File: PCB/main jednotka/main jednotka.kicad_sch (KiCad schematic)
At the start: 3 parts

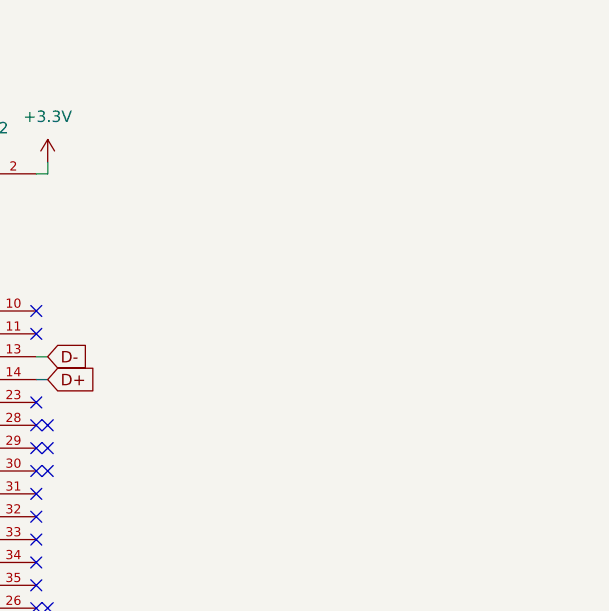
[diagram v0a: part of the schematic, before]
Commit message: USB-C + ESP32 modely added
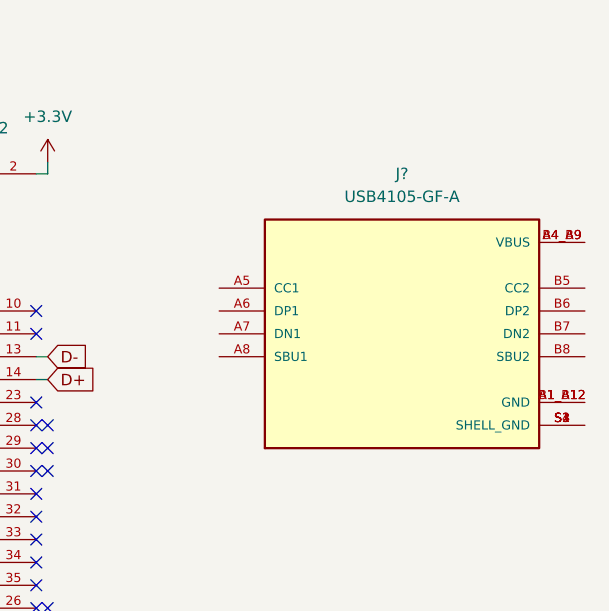
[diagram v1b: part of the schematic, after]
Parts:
- added J?: USB4105-GF-A, USB-C better:GCT_USB4105-GF-A, symbol USB4105-GF-A:USB4105-GF-A
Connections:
- new net: J?.A1_B12 (GND), J?.B1_A12 (GND)
- new net: J?.A4_B9 (VBUS), J?.B4_A9 (VBUS)
- new net: J?.S1 (SHELL_GND), J?.S2 (SHELL_GND), J?.S3 (SHELL_GND), J?.S4 (SHELL_GND)
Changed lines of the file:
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@@
     (pin "2")
+  )
+  (symbol (lib_id "USB4105-GF-A:USB4105-GF-A") (at 247.65 83.82 0) (unit 1)
+    (in_bom yes) (on_board yes) (fields_autoplaced)
+    (property "Reference" "J?" (id 0) (at 247.65 66.04 0))
+    (property "Value" "USB4105-GF-A" (id 1) (at 247.65 68.58 0))
+    (property "Footprint" "USB-C better:GCT_USB4105-GF-A" (id 2) (at 247.65 83.82 0)
+      (effects (font (size 1.27 1.27)) (justify bottom) hide)
+    )
+    (property "Datasheet" "" (id 3) (at 247.65 83.82 0)
+      (effects (font (size 1.27 1.27)) hide)
+    )
+    (property "STANDARD" "Manufacturer Recommendations" (id 4) (at 247.65 83.82 0)
+      (effects (font (size 1.27 1.27)) (justify bottom) hide)
+    )
+    (property "MAXIMUM_PACKAGE_HEIGHT" "3.31 mm" (id 5) (at 247.65 83.82 0)
+      (effects (font (size 1.27 1.27)) (justify bottom) hide)
+    )
+    (property "MANUFACTURER" "GCT" (id 6) (at 247.65 83.82 0)
+      (effects (font (size 1.27 1.27)) (justify bottom) hide)
+    )
+    (property "PARTREV" "A3" (id 7) (at 247.65 83.82 0)
+      (effects (font (size 1.27 1.27)) (justify bottom) hide)
+    )
+    (pin "A1_B12")
+    (pin "A4_B9")
+    (pin "A5")
+    (pin "A6")
+    (pin "A7")
+    (pin "A8")
+    (pin "B1_A12")
+    (pin "B4_A9")
+    (pin "B5")
+    (pin "B6")
+    (pin "B7")
+    (pin "B8")
+    (pin "S1")
+    (pin "S2")
+    (pin "S3")
+    (pin "S4")
   )
   (sheet_instances
@@
       (reference "C?") (unit 1) (value "470nF") (footprint "Capacitor_SMD:C_0805_2012Metric")
     )
+    (path "/f6eaf490-9e1f-4897-969d-df83858b4bab"
+      (reference "J?") (unit 1) (value "USB4105-GF-A") (footprint "USB-C better:GCT_USB4105-GF-A")
+    )
     (path "/e145f402-c81b-4d2e-8282-9839c39c39f7"

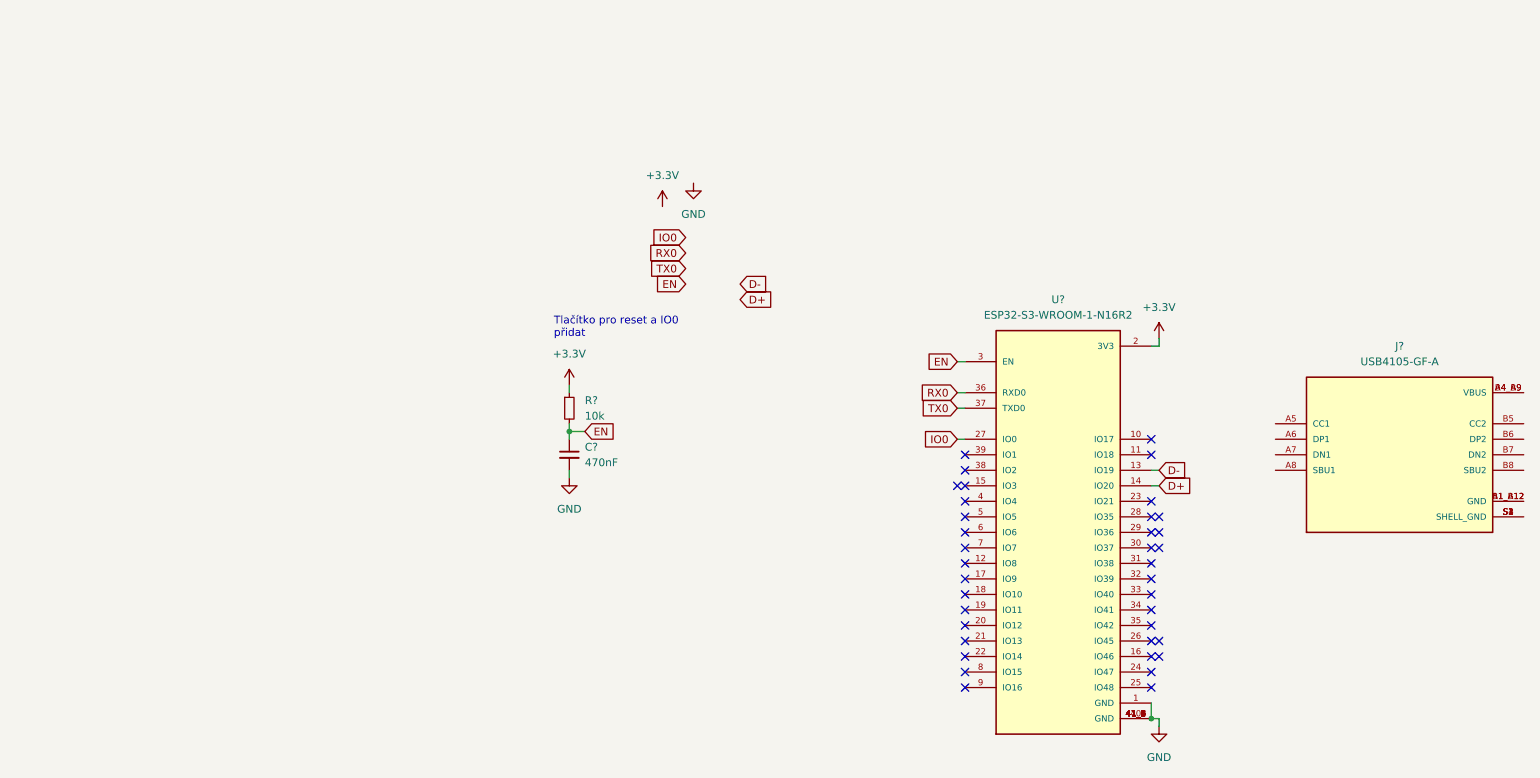
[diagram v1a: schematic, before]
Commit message: Controll boarda schéma
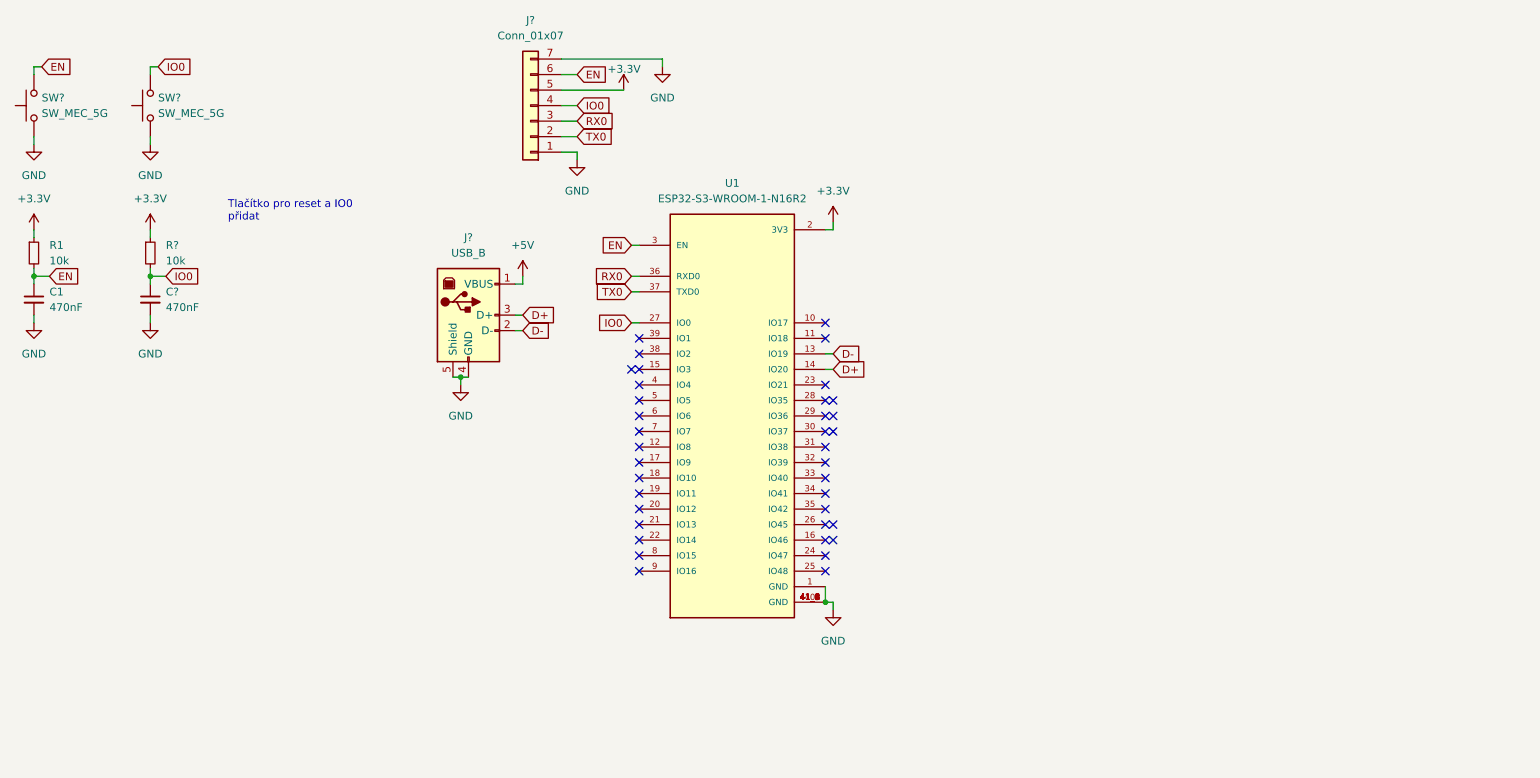
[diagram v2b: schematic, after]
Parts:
- removed J?: USB4105-GF-A, USB-C better:GCT_USB4105-GF-A, symbol USB4105-GF-A:USB4105-GF-A
- added C?: 470nF, Capacitor_SMD:C_0805_2012Metric, symbol Device:C_Small
- added J?: Conn_01x07, symbol Connector_Generic:Conn_01x07
- added J?: USB_B, symbol Connector:USB_B
- added R?: 10k, Resistor_SMD:R_0805_2012Metric, symbol Device:R_Small
- added SW? (x2): SW_MEC_5G, symbol Switch:SW_MEC_5G
- gave numbers to parts that had none: 3
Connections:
- net +3.3V: now also J?.5 (Pin_5), R?.1
- net D+: now also J?.3 (D+)
- net D-: now also J?.2 (D-)
- net EN: now also J?.6 (Pin_6), SW?.3 (B), SW?.4 (B)
- net GND: now also C?.2, J?.1 (Pin_1), J?.4 (GND), J?.5 (Shield), J?.7 (Pin_7), SW?.1 (A), SW?.1 (A), SW?.2 (A), SW?.2 (A)
- net IO0: now also C?.1, J?.4 (Pin_4), R?.2, SW?.3 (B), SW?.4 (B)
- net RX0: now also J?.3 (Pin_3)
- net TX0: now also J?.2 (Pin_2)
- new net +5V: J?.1 (VBUS)
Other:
- moved on the sheet: C1, R1, U1

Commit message: Led board + control board
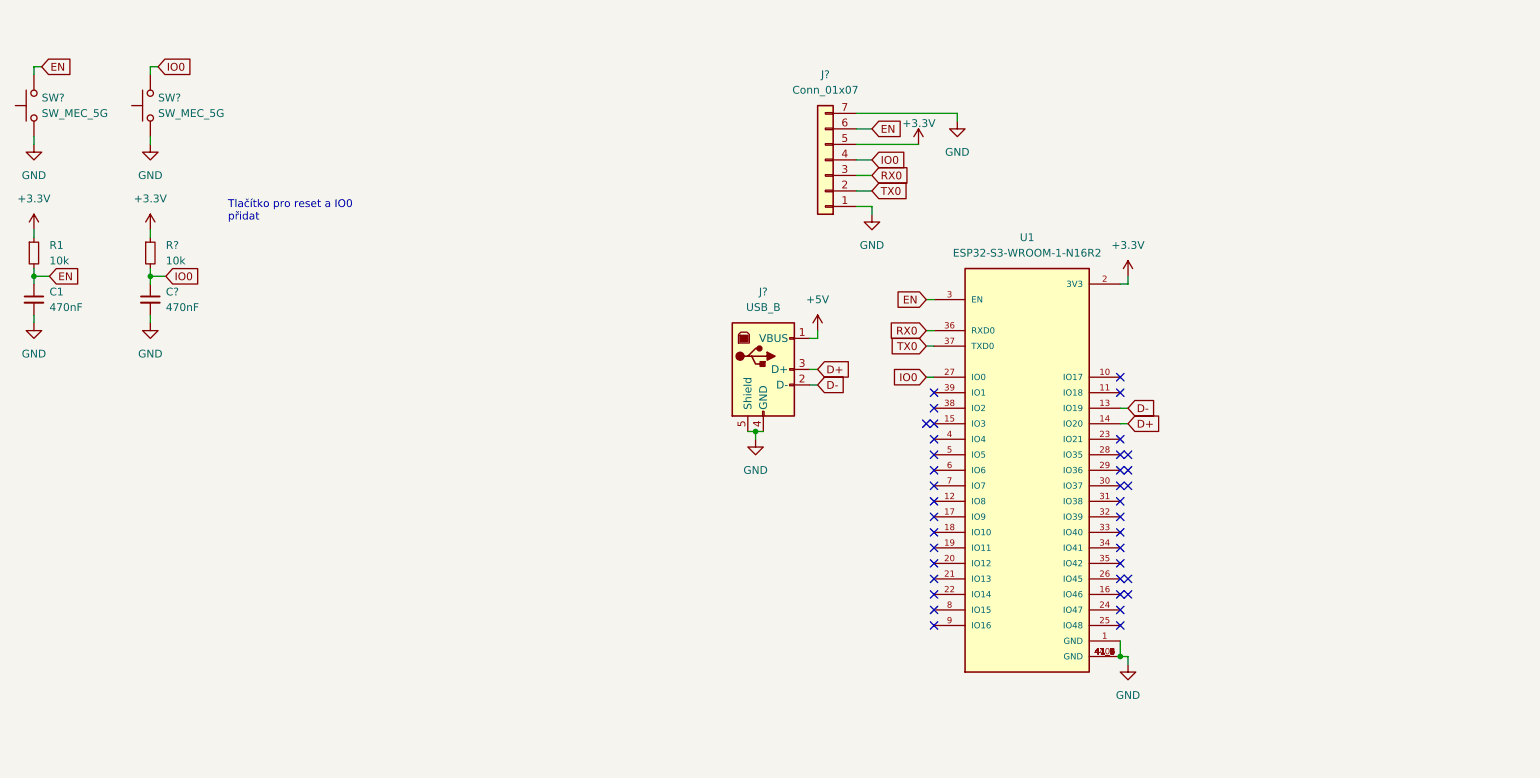
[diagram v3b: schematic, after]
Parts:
- J?: footprint (none) -> Connector_PinHeader_2.54mm:PinHeader_1x07_P2.54mm_Vertical
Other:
- moved on the sheet: J?, U1

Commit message: Main jednotka V1 a objednavka jlcpcb
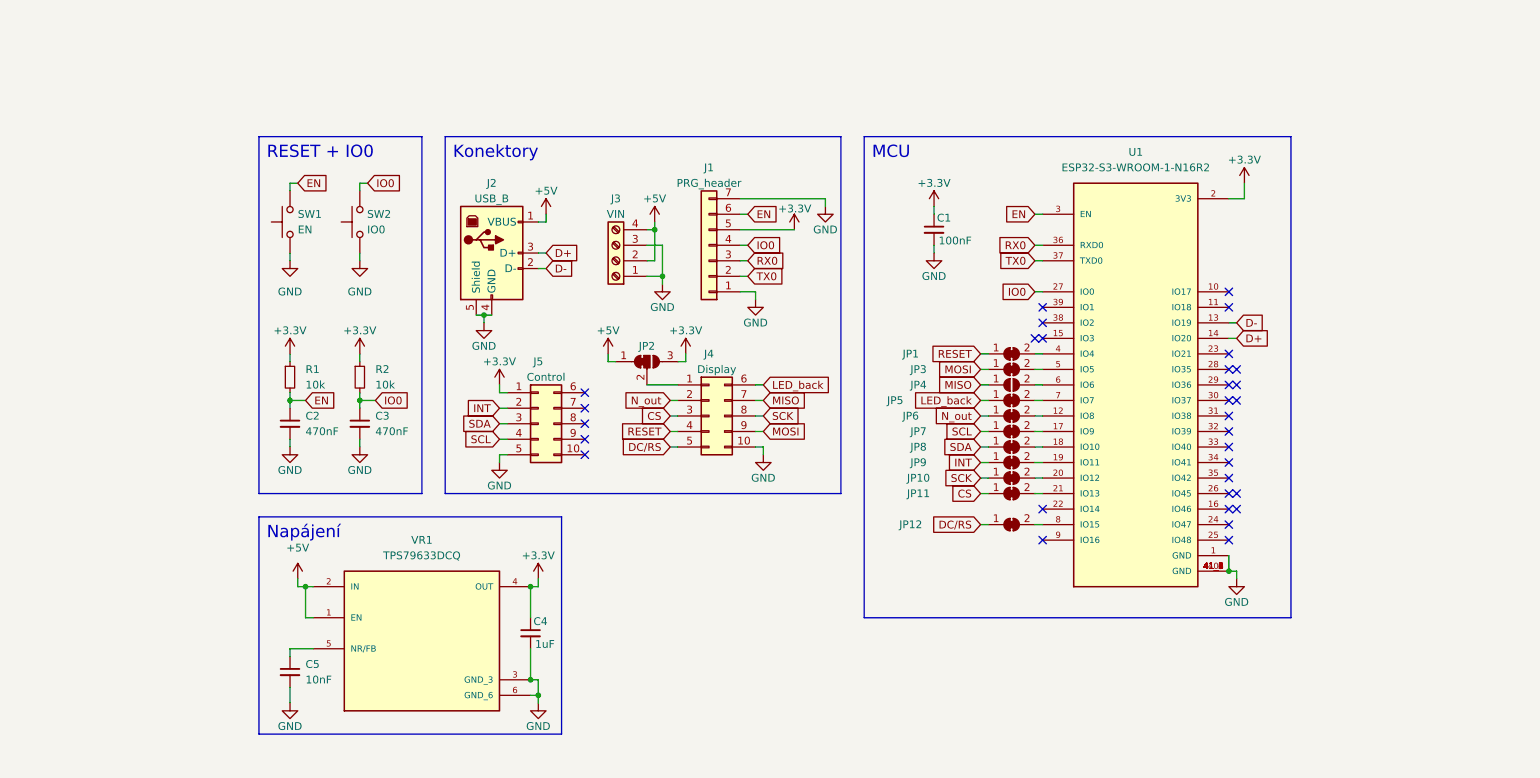
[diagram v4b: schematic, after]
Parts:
- removed SW? (x2): SW_MEC_5G, symbol Switch:SW_MEC_5G
- added C1: 100nF, Capacitor_SMD:C_0805_2012Metric_Pad1.18x1.45mm_HandSolder, symbol Device:C_Small
- added C4: 1uF, Capacitor_SMD:C_0805_2012Metric_Pad1.18x1.45mm_HandSolder, symbol Device:C_Small
- added C5: 10nF, Capacitor_SMD:C_0805_2012Metric_Pad1.18x1.45mm_HandSolder, symbol Device:C_Small
- added J3: VIN, TerminalBlock_RND:TerminalBlock_RND_205-00014_1x04_P5.00mm_Horizontal, symbol Connector:Screw_Terminal_01x04
- added J4: Display, Connector_PinSocket_2.54mm:PinSocket_2x05_P2.54mm_Vertical, symbol Connector_Generic:Conn_02x05_Top_Bottom
- added J5: Control, Connector_PinSocket_2.54mm:PinSocket_2x05_P2.54mm_Vertical, symbol Connector_Generic:Conn_02x05_Top_Bottom
- added JP1, JP10, JP11, JP12, JP3, JP5, JP6, JP7, JP8, JP9: SolderJumper_2_Bridged, Jumper:SolderJumper-2_P1.3mm_Bridged_RoundedPad1.0x1.5mm, symbol Jumper:SolderJumper_2_Bridged
- added JP2: SolderJumper_3_Bridged12, Jumper:SolderJumper-3_P1.3mm_Bridged12_RoundedPad1.0x1.5mm, symbol Jumper:SolderJumper_3_Bridged12
- added JP4: jumper, symbol Jumper:SolderJumper_2_Open
- added SW1: EN, Button_Switch_SMD:SW_SPST_CK_RS282G05A3, symbol Switch:SW_Push
- added SW2: IO0, Button_Switch_SMD:SW_SPST_CK_RS282G05A3, symbol Switch:SW_Push
- added VR1: TPS79633DCQ, TPS79633DCQ:VREG_TPS79633DCQ, symbol TP4056:TPS79633DCQ
- J1: renamed from J?; value Conn_01x07 -> PRG_header
- J2: renamed from J?; footprint (none) -> Connector_PinHeader_2.54mm:PinHeader_1x04_P2.54mm_Vertical
- gave numbers to parts that had none: 2
- renumbered C1 to C2
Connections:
- net +3.3V: now also C1.1, C4.1, J5.1 (Pin_1), JP2.3 (B), VR1.4 (OUT)
- net +5V: now also J3.2 (Pin_2), J3.4 (Pin_4), JP2.1 (A), VR1.1 (EN), VR1.2 (IN)
- net EN: now also SW1.2
- net GND: now also C1.2, C4.2, C5.2, J3.1 (Pin_1), J3.3 (Pin_3), J4.10 (Pin_10), J5.5 (Pin_5), SW1.1, SW2.1, VR1.3 (GND_3), VR1.6 (GND_6)
- net IO0: now also SW2.2
- net at U1.12 (IO8): now also JP6.2 (B)
- net at U1.17 (IO9): now also JP7.2 (B)
- net at U1.18 (IO10): now also JP8.2 (B)
- net at U1.19 (IO11): now also JP9.2 (B)
- net at U1.20 (IO12): now also JP10.2 (B)
- net at U1.21 (IO13): now also JP11.2 (B)
- net at U1.4 (IO4): now also JP1.2 (B)
- net at U1.5 (IO5): now also JP3.2 (B)
- net at U1.6 (IO6): now also JP4.2 (B)
- net at U1.7 (IO7): now also JP5.2 (B)
- net at U1.8 (IO15): now also JP12.2 (B)
- new net: J4.1 (Pin_1), JP2.2 (C)
- new net: C5.1, VR1.5 (NR/FB)
- new net CS: J4.3 (Pin_3), JP11.1 (A)
- new net DC/RS: J4.5 (Pin_5), JP12.1 (A)
- new net INT: J5.2 (Pin_2), JP9.1 (A)
- new net LED_back: J4.6 (Pin_6), JP5.1 (A)
- new net MISO: J4.7 (Pin_7), JP4.1 (A)
- new net MOSI: J4.9 (Pin_9), JP3.1 (A)
- new net N_out: J4.2 (Pin_2), JP6.1 (A)
- new net RESET: J4.4 (Pin_4), JP1.1 (A)
- new net SCK: J4.8 (Pin_8), JP10.1 (A)
- new net SCL: J5.4 (Pin_4), JP7.1 (A)
- new net SDA: J5.3 (Pin_3), JP8.1 (A)
- no-connect marks 37 -> 31
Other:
- note added: "Konektory"
- note added: "MCU"
- note added: "Napájení"
- note added: "RESET + IO0"
- note removed: "Tlačítko pro reset a IO0 přidat"
- moved on the sheet: C2, C3, J1, J2, R1, R2, U1
